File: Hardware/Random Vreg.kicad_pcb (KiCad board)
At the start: 2 copper layers, 34 x 34 mm, 17 parts, among them J1 Conn_01x07_Male, J2 Conn_01x04_Male, J3 Conn_01x02_Male, J4 Conn_01x02_Male, J5 Conn_01x02_Male, J6 Conn_01x02_Male, J7 Conn_01x08_Male, J9 QWIIC_Stackable, U1 R1501J033B-T1-JE

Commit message: whole bunche cleanup...
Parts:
- moved REF** 2.06 mm to (109.0, 87.0)
- moved G*** 2.00 mm to (91.0, 86.0)
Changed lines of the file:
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@@
   )
   (footprint "Tinker:DagNabbit" (layer "F.Cu")
-    (at 107 86.5)
+    (at 109 87)
     (attr smd board_only)
     (fp_text reference "REF**" (at 0 -8.08 unlocked) (layer "F.SilkS") hide
@@
   )
   (footprint "Tinker:NerdMage" (layer "F.Cu")
-    (at 93 85.9)
+    (at 91 86)
     (attr board_only exclude_from_pos_files exclude_from_bom)
     (fp_text reference "G***" (at 0 3.81) (layer "F.SilkS") hide

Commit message: Still migrating to 0.2.x
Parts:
- removed J1: Conn_01x07_Male, Tinker:Board_Stacker_7
- moved C2 1.65 mm to (108.1, 91.2)
- moved U1 1.65 mm to (108.1, 101.1)
- moved C1 1.65 mm to (108.9, 93.9)
- moved J6 1.28 mm to (114.0, 92.4)
- moved J5 0.66 mm to (114.0, 99.4)
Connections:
- net ALERT renamed ~{SCS}0
- net GPIO renamed MOSI
- net POWER_OK2 renamed SCLK
- net POWER_OK3 renamed MISO
- J7 pad 1: RESET -> ~{RESET}
- J7 pad 2: ATTACH -> RESET
- J7 pad 3: SCL -> ~{SCS}2
- J7 pad 5: SDA -> ~{SCS}1
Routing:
- net Vout: track 57.2 -> 69.8 mm
- net SDA: track 10.6 -> 0.00 mm
- net SCL: track 6.15 -> 0.00 mm
- net Vsec: track 26.5 -> 23.0 mm, vias 0 -> 1
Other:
- board text added: "2,1,0"
- board text added: ">RST"
- board text added: ">~{RST}"
- board text added: "MISO"
- board text added: "MOSI"
- board text added: "SCL"
- board text added: "SCLK"
- board text added: "SDA"
- board text added: "SPI"
- board text added: "USB"
- board text added: "Vusb"
- board text added: "~{SCS}"
- board text removed: "DTR"
- board text removed: "RST"
- board text removed: "RTS"
- board text removed: "RxD"
- board text removed: "TxD"

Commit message: ...
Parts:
- added J10: Conn_01x02_Male, Tinker:Board_Stacker_2, F.Cu at (99.4, 114.0)
- moved C2 0.25 mm to (107.9, 91.2)
- moved U1 0.18 mm to (107.9, 101.0)
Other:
- board text added: "Vrnd"
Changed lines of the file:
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@@
   (net 15 "~{SCS}0")
   (net 16 "MOSI")
+  (net 17 "unconnected-(J10-Pad1)")
+  (net 18 "unconnected-(J10-Pad2)")
   (footprint "Tinker:Mount" (layer "F.Cu")
     (at 114 114)
@@
   )
   (footprint "Tinker:CP_EIA-6032-28-Tantalumm_HandSolder" (layer "F.Cu")
-    (at 108.146545 91.24)
+    (at 107.9 91.24)
     (descr "Tantalum Capacitor SMD Kemet-C (6032-28 Metric), IPC_7351 nominal, (Body size from: http://www.kemet.com/Lists/ProductCatalog/Attachments/253/KEM_TC101_STD.pdf), generated with kicad-footprint-generator")
     (tags "capacitor tantalum")
@@
       ) (layer "F.SilkS") (width 0) (fill solid))
   )
+  (footprint "Tinker:Board_Stacker_2" (layer "F.Cu")
+    (at 99.365 114 90)
+    (descr "JST SH series connector, SM04B-SRSS-TB (http://www.jst-mfg.com/product/pdf/eng/eSH.pdf), generated with kicad-footprint-generator")
+    (tags "connector JST SH top entry")
+    (property "Sheetfile" "Random Vreg.kicad_sch")
+    (property "Sheetname" "")
+    (property "exclude_from_bom" "")
+    (attr smd exclude_from_bom)
+    (fp_text reference "J10" (at 1.6 0.635) (layer "F.SilkS")
+      (effects (font (size 0.6 0.6) (thickness 0.15)))
+    )
+    (fp_text value "Conn_01x02_Male" (at 0 4.084197 90) (layer "F.Fab")
+      (effects (font (size 1 1) (thickness 0.15)))
+    )
+    (fp_line (start 2 -0.645) (end -2 -0.645) (layer "F.CrtYd") (width 0.05))
+    (fp_line (start -2 -0.645) (end -2 1.915) (layer "F.CrtYd") (width 0.05))
+    (fp_line (start 2 1.915) (end 2 -0.645) (layer "F.CrtYd") (width 0.05))
+    (fp_line (start -2 1.915) (end 2 1.915) (layer "F.CrtYd") (width 0.05))
+    (fp_line (start -1.020528 -0.11) (end -0.495528 -0.635) (layer "F.Fab") (width 0.1))
+    (fp_line (start -0.495528 -0.635) (end 1.079472 -0.635) (layer "F.Fab") (width 0.1))
+    (fp_line (start -1.020528 1.905) (end -1.020528 -0.11) (layer "F.Fab") (width 0.1))
+    (fp_line (start 1.079472 -0.635) (end 1.079472 1.905) (layer "F.Fab") (width 0.1))
+    (fp_line (start 1.079472 1.905) (end -1.020528 1.905) (layer "F.Fab") (width 0.1))
+    (pad "1" smd rect (at 1.35 0 90) (size 1.8 0.65) (layers "B.Cu" "B.Paste" "B.Mask")
+      (net 17 "unconnected-(J10-Pad1)") (pinfunction "Pin_1") (pintype "passive"))
+    (pad "1" thru_hole rect (at 0 0 90) (size 1 1) (drill 0.65) (layers *.Cu *.Mask)
+      (net 17 "unconnected-(J10-Pad1)") (pinfunction "Pin_1") (pintype "passive"))
+    (pad "2" smd rect (at -1.35 1.27 90) (size 1.8 0.65) (layers "B.Cu" "B.Paste" "B.Mask")
+      (net 18 "unconnected-(J10-Pad2)") (pinfunction "Pin_2") (pintype "passive"))
+    (pad "2" thru_hole oval (at 0 1.27 90) (size 1 1) (drill 0.65) (layers *.Cu *.Mask)
+      (net 18 "unconnected-(J10-Pad2)") (pinfunction "Pin_2") (pintype "passive"))
+    (model "${KICAD6_3DMODEL_DIR}/Connector_PinHeader_1.27mm.3dshapes/PinHeader_1x02_P1.27mm_Vertical.step"
+      (offset (xyz 0 0 0))
+      (scale (xyz 1 1 1))
+      (rotate (xyz 0 0 0))
+    )
+    (model "${KICAD6_3DMODEL_DIR}/Connector_PinSocket_1.27mm.3dshapes/PinSocket_1x02_P1.27mm_Vertical_SMD_Pin1Left.step"
+      (offset (xyz 0 -0.635 -1.72))
+      (scale (xyz 1 1 1))
+      (rotate (xyz 0 -180 0))
+    )
+    (model "${KICAD6_3DMODEL_DIR}/Connector_PinSocket_1.27mm.3dshapes/PinSocket_1x02_P1.27mm_Vertical.step" hide
+      (offset (xyz 0 0 -1.72))
+      (scale (xyz 1 1 1))
+      (rotate (xyz 0 180 0))
+    )
+  )
   (footprint "Tinker:R1501J033BT1JE" (layer "F.Cu")
-    (at 108.058834 101.084151 180)
+    (at 107.9 101 180)
     (descr "TO-252-5-P2_2023")
     (tags "Integrated Circuit")
@@
   )
   (footprint "Capacitor_SMD:C_0603_1608Metric" (layer "F.Cu")
-    (at 108.921545 93.9)
+    (at 108.9 93.9)
     (descr "Capacitor SMD 0603 (1608 Metric), square (rectangular) end terminal, IPC_7351 nominal, (Body size source: IPC-SM-782 page 76, https://www.pcb-3d.com/wordpress/wp-content/uploads/ipc-sm-782a_amendment_1_and_2.pdf), generated with kicad-footprint-generator")
     (tags "capacitor")
@@
     (effects (font (size 0.6 0.6) (thickness 0.125)) (justify right))
   )
+  (gr_text "Vrnd" (at 100 116.2) (layer "F.SilkS")
+    (effects (font (size 1 1) (thickness 0.15)))
+  )
   (gr_text "I2C" (at 83.8 93 -90) (layer "F.SilkS")
     (effects (font (size 1 1) (thickness 0.15)))
@@
     (effects (font (size 1 1) (thickness 0.15)))
   )
-  (segment (start 110.232391 95.130799) (end 110.598834 95.497242) (width 0.6) (layer "F.Cu") (net 4))
+  (segment (start 110.44 95.645) (end 109.925799 95.130799) (width 0.6) (layer "F.Cu") (net 4))
   (segment (start 108.146545 94.898721) (end 107.914467 95.130799) (width 0.6) (layer "F.Cu") (net 4))
-  (segment (start 110.598834 95.497242) (end 110.598834 97.009151) (width 0.6) (layer "F.Cu") (net 4))
-  (segment (start 106.788834 97.009151) (end 106.788834 95.621763) (width 0.6) (layer "F.Cu") (net 4))
+  (segment (start 106.63 95.780597) (end 106.788834 95.621763) (width 0.6) (layer "F.Cu") (net 4))
   (segment (start 106.788834 95.621763) (end 107.279798 95.130799) (width 0.6) (layer "F.Cu") (net 4))
   (segment (start 108.146545 93.9) (end 108.146545 87.940003) (width 0.6) (layer "F.Cu") (net 4))
+  (segment (start 110.44 96.925) (end 110.44 95.645) (width 0.6) (layer "F.Cu") (net 4))
   (segment (start 108.146545 87.940003) (end 106.206542 86) (width 0.6) (layer "F.Cu") (net 4))
+  (segment (start 106.63 96.925) (end 106.63 95.780597) (width 0.6) (layer "F.Cu") (net 4))
   (segment (start 106.206542 86) (end 101.905 86) (width 0.6) (layer "F.Cu") (net 4))
   (segment (start 108.146545 93.9) (end 108.146545 94.898721) (width 0.6) (layer "F.Cu") (net 4))
   (segment (start 107.279798 95.130799) (end 107.914467 95.130799) (width 0.6) (layer "F.Cu") (net 4))
-  (segment (start 107.914467 95.130799) (end 110.232391 95.130799) (width 0.6) (layer "F.Cu") (net 4))
+  (segment (start 109.925799 95.130799) (end 107.914467 95.130799) (width 0.6) (layer "F.Cu") (net 4))
   (segment (start 114 106.365) (end 101.801977 106.365) (width 0.6) (layer "B.Cu") (net 4))
   (segment (start 101.905 106.261977) (end 101.801977 106.365) (width 0.6) (layer "B.Cu") (net 4))
   (segment (start 101.905 86) (end 101.905 106.261977) (width 0.6) (layer "B.Cu") (net 4))
   (segment (start 101.801977 106.365) (end 86 106.365) (width 0.6) (layer "B.Cu") (net 4))
+  (segment (start 105.35 92.601166) (end 105.35 91.24) (width 0.6) (layer "F.Cu") (net 14))
   (segment (start 114.410868 99.365) (end 114 99.365) (width 0.6) (layer "F.Cu") (net 14))
+  (segment (start 105.36 96.925) (end 105.36 92.611166) (width 0.6) (layer "F.Cu") (net 14))
   (segment (start 114.618557 92.365) (end 115.232285 92.978728) (width 0.6) (layer "F.Cu") (net 14))
   (segment (start 115.232285 92.978728) (end 115.232285 98.543583) (width 0.6) (layer "F.Cu") (net 14))
-  (segment (start 105.518834 97.009151) (end 105.518834 92.601166) (width 0.6) (layer "F.Cu") (net 14))
-  (segment (start 105.518834 91.317711) (end 105.596545 91.24) (width 0.6) (layer "F.Cu") (net 14))
   (segment (start 114 92.365) (end 114.618557 92.365) (width 0.6) (layer "F.Cu") (net 14))
   (segment (start 115.232285 98.543583) (end 114.410868 99.365) (width 0.6) (layer "F.Cu") (net 14))
-  (segment (start 105.518834 92.601166) (end 105.518834 91.317711) (width 0.6) (layer "F.Cu") (net 14))
-  (via (at 105.518834 92.601166) (size 0.8) (drill 0.4) (layers "F.Cu" "B.Cu") (net 14))
+  (segment (start 105.36 92.611166) (end 105.35 92.601166) (width 0.6) (layer "F.Cu") (net 14))
+  (via (at 105.35 92.601166) (size 0.8) (drill 0.4) (layers "F.Cu" "B.Cu") (net 14))
   (segment (start 114 92.365) (end 105.755 92.365) (width 0.6) (layer "B.Cu") (net 14))
   (segment (start 105.755 92.365) (end 105.518834 92.601166) (width 0.6) (layer "B.Cu") (net 14))

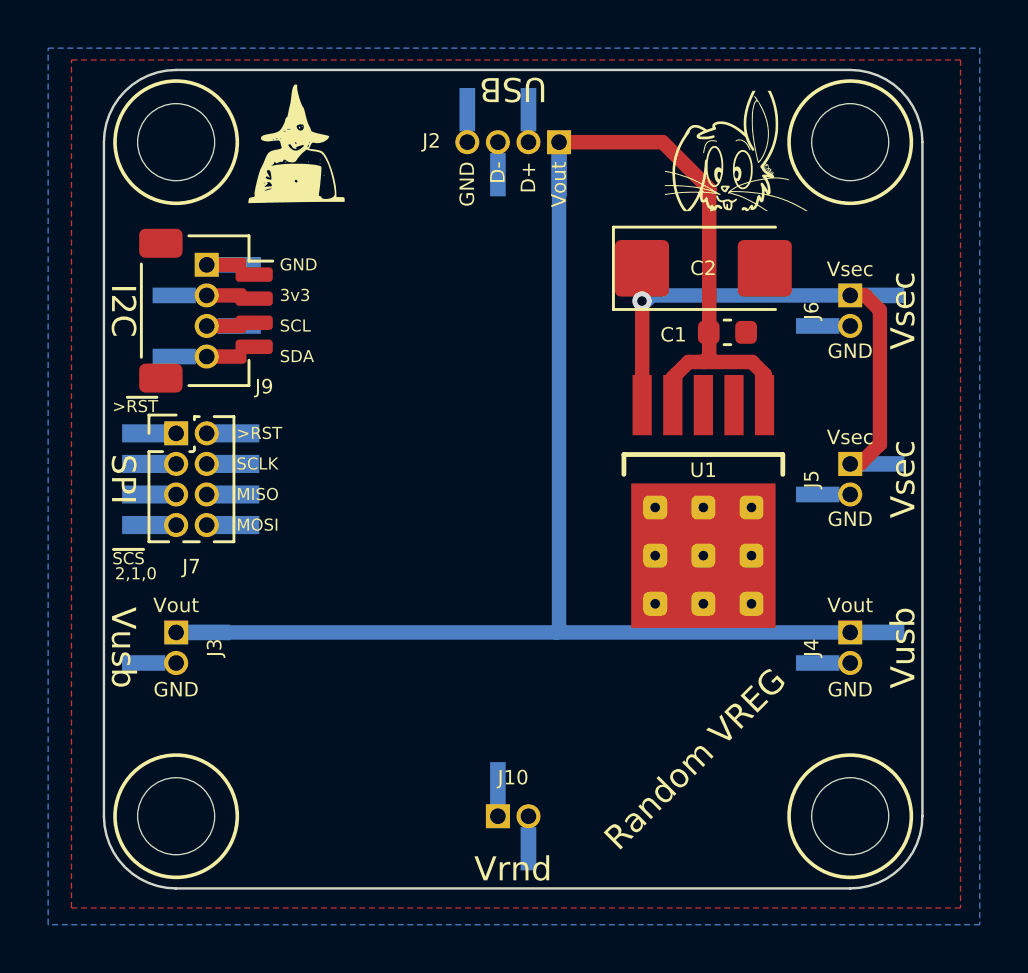
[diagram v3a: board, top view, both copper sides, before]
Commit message: Re-doing Random VREG
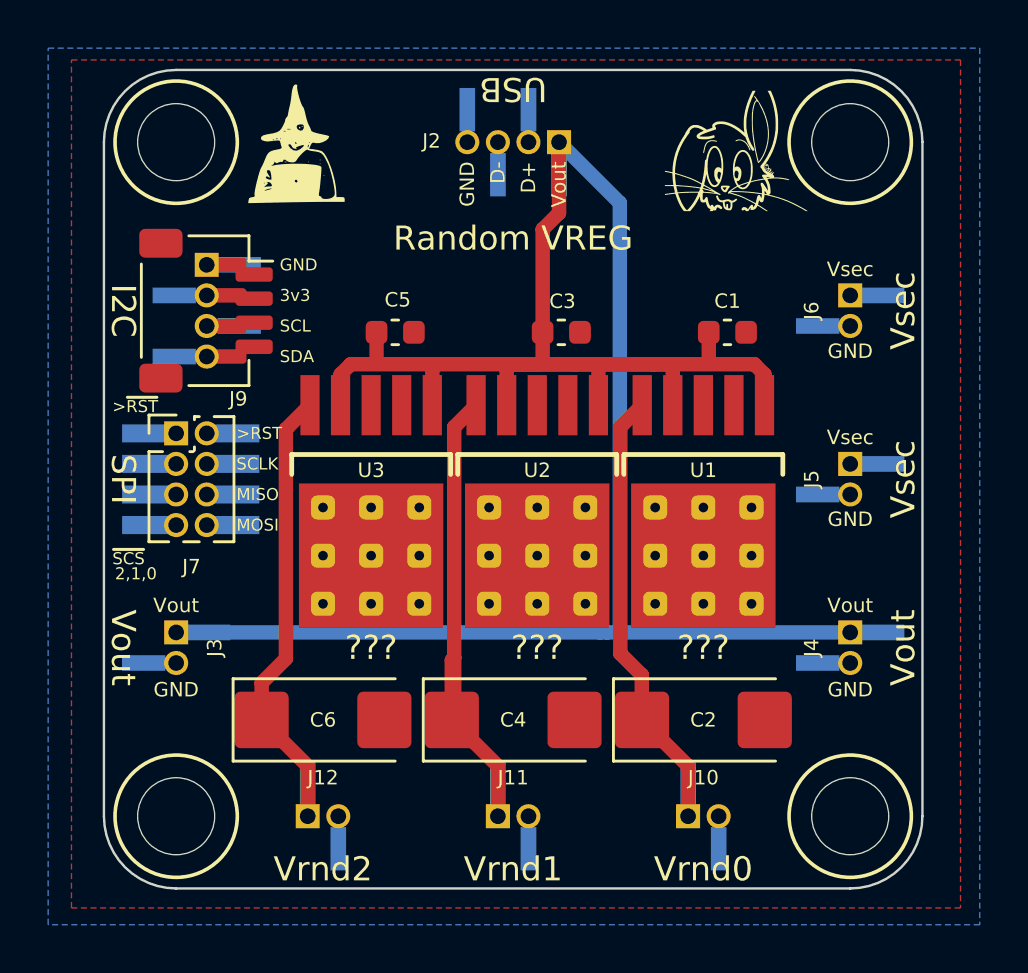
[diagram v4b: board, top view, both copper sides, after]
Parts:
- added C3: 1.0uF, Capacitor_SMD:C_0603_1608Metric, F.Cu at (102.0, 93.9)
- added C4: 22uf, Tinker:CP_EIA-6032-28-Tantalumm_HandSolder, F.Cu at (100.0, 110.0)
- added C5: 1.0uF, Capacitor_SMD:C_0603_1608Metric, F.Cu at (95.1, 93.9)
- added C6: 22uf, Tinker:CP_EIA-6032-28-Tantalumm_HandSolder, F.Cu at (92.1, 110.0)
- added J10: Conn_01x02_Male, Tinker:Board_Stacker_2, F.Cu at (107.3, 114.0)
- added J12: Conn_01x02_Male, Tinker:Board_Stacker_2, F.Cu at (91.5, 114.0)
- added U2: R1501J033B-T1-JE, Tinker:R1501J033BT1JE, F.Cu at (101.0, 101.0)
- added U3: R1501J033B-T1-JE, Tinker:R1501J033BT1JE, F.Cu at (94.1, 101.0)
- moved C2 18.8 mm to (107.9, 110.0)
- renumbered J10 to J11
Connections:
- C2 pad 1: Vsec -> /Vrnd0
- J11 pad 1: unconnected-(J10-Pad1) -> /Vrnd1
- J11 pad 2: unconnected-(J10-Pad2) -> GND
- J5 pad 1: Vsec -> unconnected-(J5-Pad1)
- J6 pad 1: Vsec -> unconnected-(J6-Pad1)
- U1 pad 5: Vsec -> /Vrnd0
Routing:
- net Vout: track 69.5 -> 95.6 mm
- net Vsec: track 22.9 -> 0.00 mm, vias 1 -> 0
- net /Vrnd1: track 0.00 -> 20.0 mm
- net /Vrnd2: track 0.00 -> 18.7 mm
- net /Vrnd0: track 0.00 -> 18.6 mm
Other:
- board text added: "???"
- board text added: "Vrnd0"
- board text added: "Vrnd1"
- board text added: "Vrnd2"
- board text removed: "Vrnd"
- board text removed: "Vusb"

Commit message: Random VREG!
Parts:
- added C7: 100nf, Capacitor_SMD:C_0603_1608Metric, F.Cu at (98.8, 91.7)
- added R1: 10K, Resistor_SMD:R_0603_1608Metric, F.Cu at (98.8, 93.2)
- added R2: 10K, Resistor_SMD:R_0603_1608Metric, F.Cu at (95.8, 107.4)
- added R3: 10K, Resistor_SMD:R_0603_1608Metric, F.Cu at (102.7, 107.4)
- added R4: 10K, Resistor_SMD:R_0603_1608Metric, F.Cu at (109.6, 107.4)
- added R5: 10K, Resistor_SMD:R_0603_1608Metric, F.Cu at (104.0, 93.0)
- added R6: 10K, Resistor_SMD:R_0603_1608Metric, F.Cu at (104.0, 91.5)
- added R7: 10K, Resistor_SMD:R_0603_1608Metric, F.Cu at (104.0, 90.0)
- added U4: PCA9557BS, Package_DFN_QFN:HVQFN-16-1EP_3x3mm_P0.5mm_EP1.5x1.5mm, F.Cu at (95.0, 92.0)
- moved C1 13.8 mm to (92.3, 107.4)
- moved C2 13.8 mm to (99.2, 107.4)
- moved C3 13.8 mm to (106.1, 107.4)
- turned U1 to 0 degrees
- turned U2 to 0 degrees
- turned U3 to 0 degrees
- renumbered C5 to C1, C3 to C2, C1 to C3, C6 to C4, C4 to C5, C2 to C6, J12 to J10, J10 to J12, U3 to U1, U1 to U3
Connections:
- U1 pad 4: Vout -> CE0
- U2 pad 4: Vout -> CE1
- U3 pad 4: Vout -> CE2
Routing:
- net Vout: track 95.6 -> 58.3 mm, vias 0 -> 3
- net CE2: track 0.00 -> 34.7 mm
- net CE1: track 0.00 -> 33.0 mm
- net CE0: track 0.00 -> 27.5 mm
- net GND: track 0.00 -> 17.5 mm, vias 0 -> 1
- net Vcc?: track 0.00 -> 16.5 mm, vias 0 -> 1
- net SCL: track 0.00 -> 11.7 mm, vias 0 -> 1
- net SDA: track 0.00 -> 10.3 mm, vias 0 -> 1
- net A2: track 0.00 -> 9.80 mm
- net A1: track 0.00 -> 9.55 mm
- net A0: track 0.00 -> 9.27 mm
- net /Vrnd1: track 20.0 -> 14.1 mm, vias 0 -> 1
- net /Vrnd0: track 18.6 -> 13.7 mm, vias 0 -> 1
- net /Vrnd2: track 18.7 -> 14.5 mm, vias 0 -> 1
- net Net-(R1-Pad2): track 0.00 -> 1.60 mm
